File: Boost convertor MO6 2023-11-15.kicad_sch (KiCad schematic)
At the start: 26 parts, among them J1 Screw_Terminal_01x02, J2 Screw_Terminal_01x02, Q1 IRLZ44N, Q2 BC547, U1 MCP6002-xMC, U2 MCP6002-xMC, U3 L7805

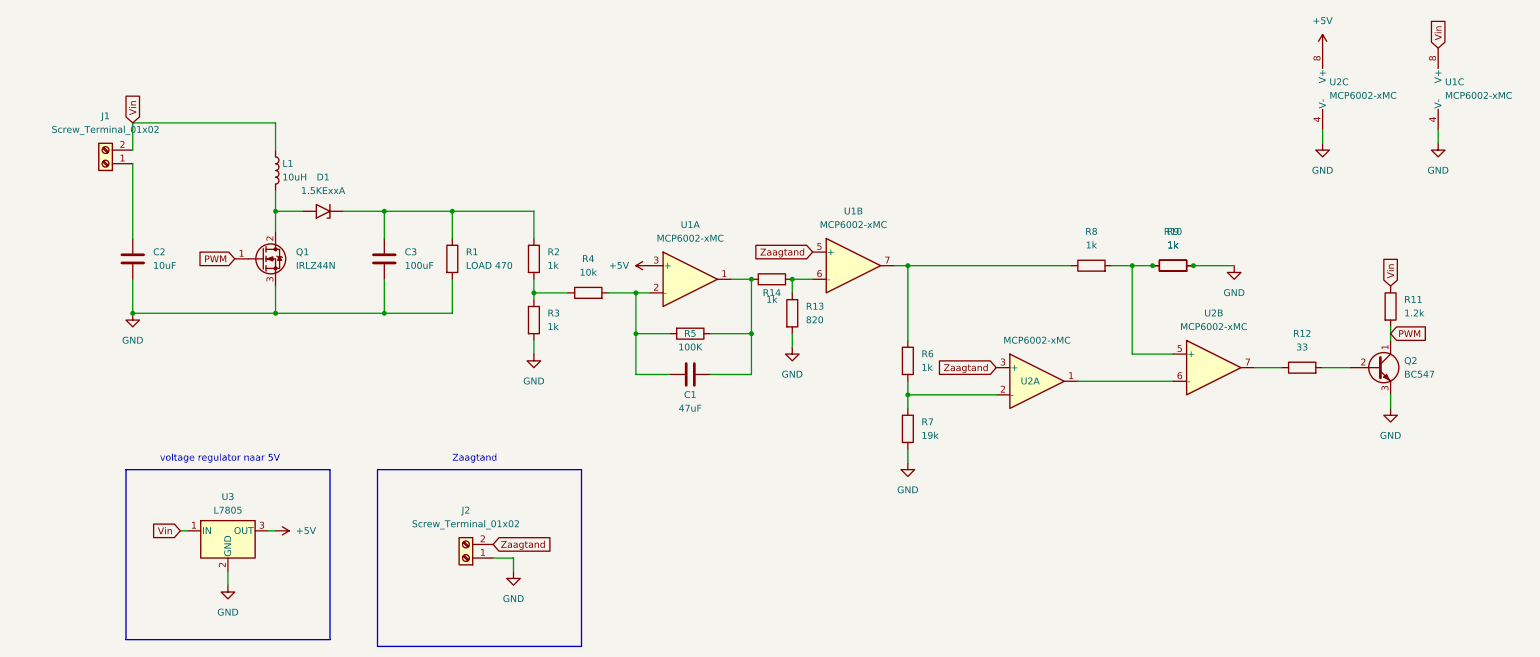
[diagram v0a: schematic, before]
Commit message: load verwijderd
Ik heb de load verwijdert, want daar komt het systeem van de controllers aan te hangen.
Verder heb ik C2 parallel gezet aan J1. Dit kan ik eerst in serie, maar dat was niet mijn bedoeling.
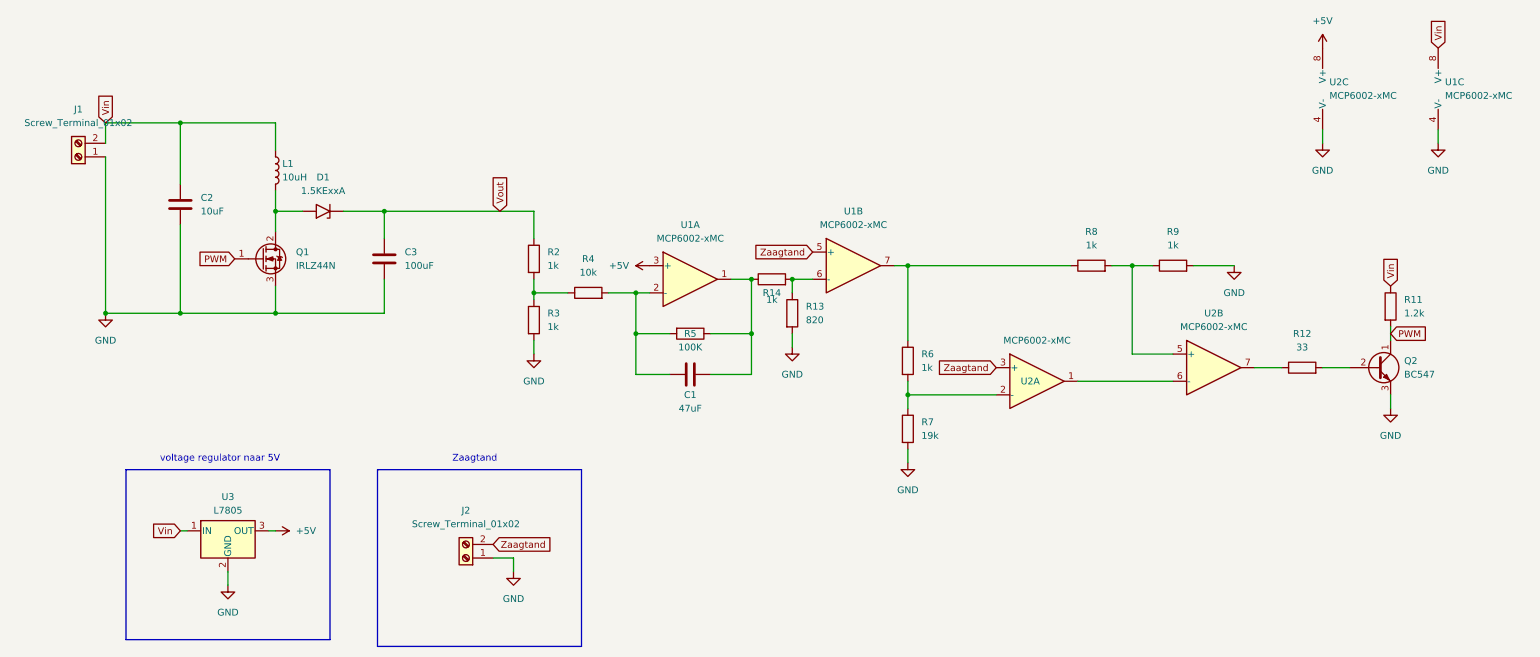
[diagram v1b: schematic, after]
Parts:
- removed R1: LOAD 470, symbol Device:R
- removed R10: 1k, symbol Device:R
- C1, C2, C3: footprint (none) -> Capacitor_SMD:C_0805_2012Metric_Pad1.18x1.45mm_HandSolder
- J1, J2: footprint (none) -> TerminalBlock:TerminalBlock_Altech_AK300-2_P5.00mm
- L1: footprint (none) -> Inductor_SMD:L_7.3x7.3_H4.5
- R11, R12, R13, R14, R2, R3, R4, R5, R6, R7, R8, R9: footprint (none) -> Resistor_SMD:R_0805_2012Metric_Pad1.20x1.40mm_HandSolder
- U3: footprint (none) -> Package_SO:SOIC-8-1EP_3.9x4.9mm_P1.27mm_EP2.29x3mm
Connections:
- net GND: now also J1.1 (Pin_1)
- net Vin: now also C2.2
- net Vout: now reaches C3.2, D1.1 (A1), R2.1
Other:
- moved on the sheet: C2, J1
